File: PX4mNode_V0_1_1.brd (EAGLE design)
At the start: 48.6 x 34.9 mm, 135 parts, among them J201 DF13C-6P-1.25V, J202 DF13C-6P-1.25V, J203 DF13C-6P-1.25V, J301 DF13C-4P-1.25V, J401 DF13C-7P-1.25V, J402 DF13-4P-1.25V, J403 DF13C-4P-1.25V, J404 DF13C-4P-1.25V, J405 DF13C-4P-1.25V, J801 DF13C-3P-1.25V, M3_MOUNT1101 MOUNT-HOLE3.1MM, M3_MOUNT1102 MOUNT-HOLE3.1MM, M3_MOUNT1103 MOUNT-HOLE3.1MM, M3_MOUNT1104 MOUNT-HOLE3.1MM, U101 STM32F4X7VX, U401 MAX3051, U402 MAX3051, X101 3.2x2.5 mm / 24 MHz / 15 ppm

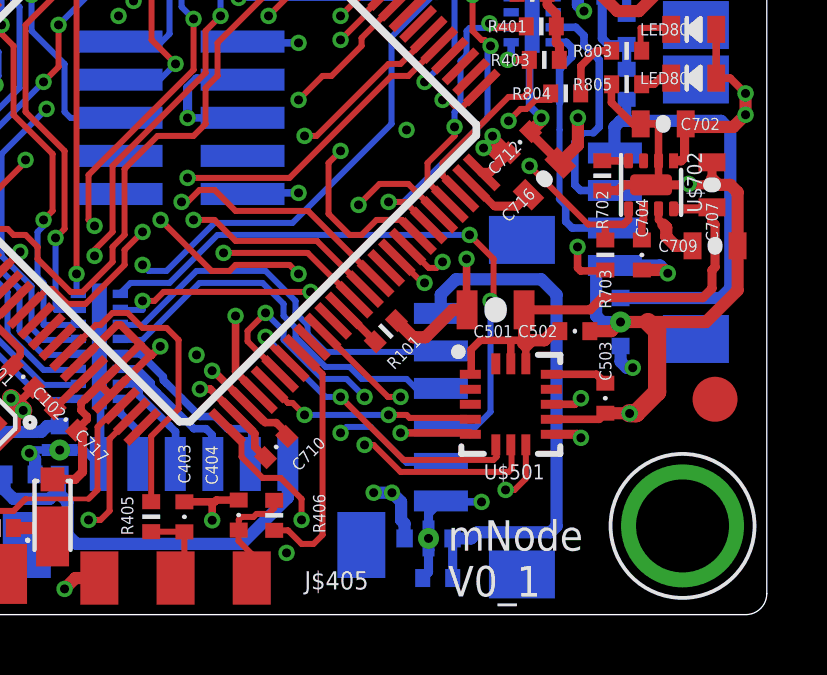
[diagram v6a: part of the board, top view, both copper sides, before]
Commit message: Part renumbering again
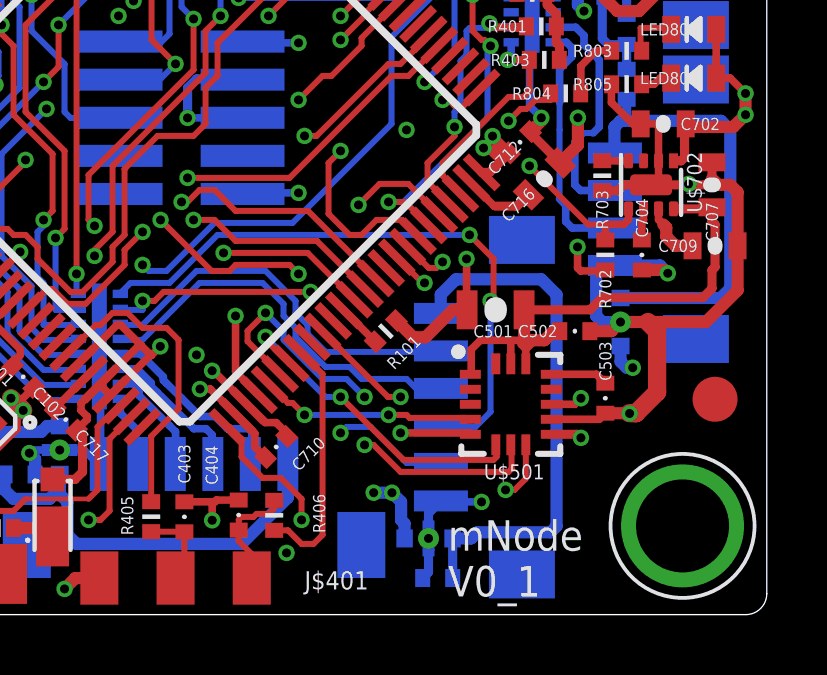
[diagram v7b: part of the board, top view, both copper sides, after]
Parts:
- removed JP2, JP3: FIDUCIAL1.5X3, pixhawk2:FIDUCIAL-1.5X3
- removed U$1: 74LVC2GU04, pixhawk2:SOT363_PHILIPS
- added JP1103, JP1104: FIDUCIAL1.5X3, pixhawk2:FIDUCIAL-1.5X3
- added U$205: PESD0402-140, pixhawk2:0402-TVS
- U$202: value PESD0402-140 -> 74LVC2GU04; device pixhawk2:0402-TVS -> pixhawk2:SOT363_PHILIPS
- moved JP1101 33.0 mm to (51.2, 30.9), flipped to the bottom
- moved U$202 26.1 mm to (22.0, 12.1), turned to 270 degrees
- moved JP1102 25.2 mm to (30.9, 10.2), flipped to the bottom
- moved U$203 14.3 mm to (46.8, 3.96), turned to 0 degrees
- moved U$204 13.0 mm to (32.9, 7.42), turned to 180 degrees
- moved L201 9.08 mm to (35.6, 11.7), turned to 90 degrees
- moved L202 9.08 mm to (26.5, 10.9), turned to 180 degrees
- moved R702 2.64 mm to (52.4, 14.7)
- moved R703 2.64 mm to (52.3, 17.4)
- renumbered C1 to C201, D1 to D701, J$405 to J$401, JP1 to JP201, JP4 to JP202, U$602 to U$601
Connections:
- net 5V_S1_FILTERED: now also U$203.C; no longer U$202.C
- net 5V_S2_FILTERED: now also U$204.C; no longer U$203.C
- net 5V_S3_FILTERED: now also U$205.C; no longer U$204.C
- net FMU-UART7_RX: now also L202.P$5; no longer L201.P$5
- net FMU-UART7_TX: now also L202.P$7; no longer L201.P$7
- net FMU-UART8_RX: now also U$202.6; no longer U$1.6
- net FMU-UART8_TX: now also U$202.3; no longer U$1.3
- net FMU-USART2_CTS: now also L201.P$8; no longer L202.P$8
- net FMU-USART2_RTS: now also L201.P$7; no longer L202.P$7
- net FMU-USART2_RX: now also L201.P$5; no longer L202.P$5
- net FMU-USART2_TX: now also L201.P$6; no longer L202.P$6
- net FMU-USART3_CTS: now also L201.P$2; no longer L202.P$2
- net FMU-USART3_RTS: now also L201.P$1; no longer L202.P$1
- net FMU-USART3_RX: now also L201.P$3; no longer L202.P$3
- net FMU-USART3_TX: now also L201.P$4; no longer L202.P$4
- net FMU-VDD_3V3: now also R702.P$1, U$202.5; no longer R703.P$1, U$1.5
- net GND: now also L202.P$1, L202.P$15, L202.P$16, L202.P$2, R703.P$1, U$202.2, U$205.A; no longer L201.P$1, L201.P$15, L201.P$16, L201.P$2, R702.P$1, U$1.2, U$202.A
- net N$18: now also L202.P$13, L202.P$14; no longer L201.P$13, L201.P$14
- net N$5: now also U$202.4; no longer U$1.4
- net PPM_INPUT: now also L202.P$3, U$202.1; no longer L201.P$3, U$1.1
- net SERIAL1_CTS: now also L201.P$9; no longer L202.P$9
- net SERIAL1_RTS: now also L201.P$10; no longer L202.P$10
- net SERIAL1_RX: now also L201.P$12; no longer L202.P$12
- net SERIAL1_TX: now also L201.P$11; no longer L202.P$11
- net SERIAL2_CTS: now also L201.P$15; no longer L202.P$15
- net SERIAL2_RTS: now also L201.P$16; no longer L202.P$16
- net SERIAL2_RX: now also L201.P$14; no longer L202.P$14
- net SERIAL2_TX: now also L201.P$13; no longer L202.P$13
- net SERIAL3_RX: now also L202.P$12; no longer L201.P$12
- net SERIAL3_TX: now also L202.P$10; no longer L201.P$10
- net SPEKTRUM_RX: now also L202.P$4; no longer L201.P$4
- net VDD_3V3_PERIPH_EN: now also R703.P$2; no longer R702.P$2
- net VDD_3V3_SENSORS_EN: now also R702.P$2; no longer R703.P$2

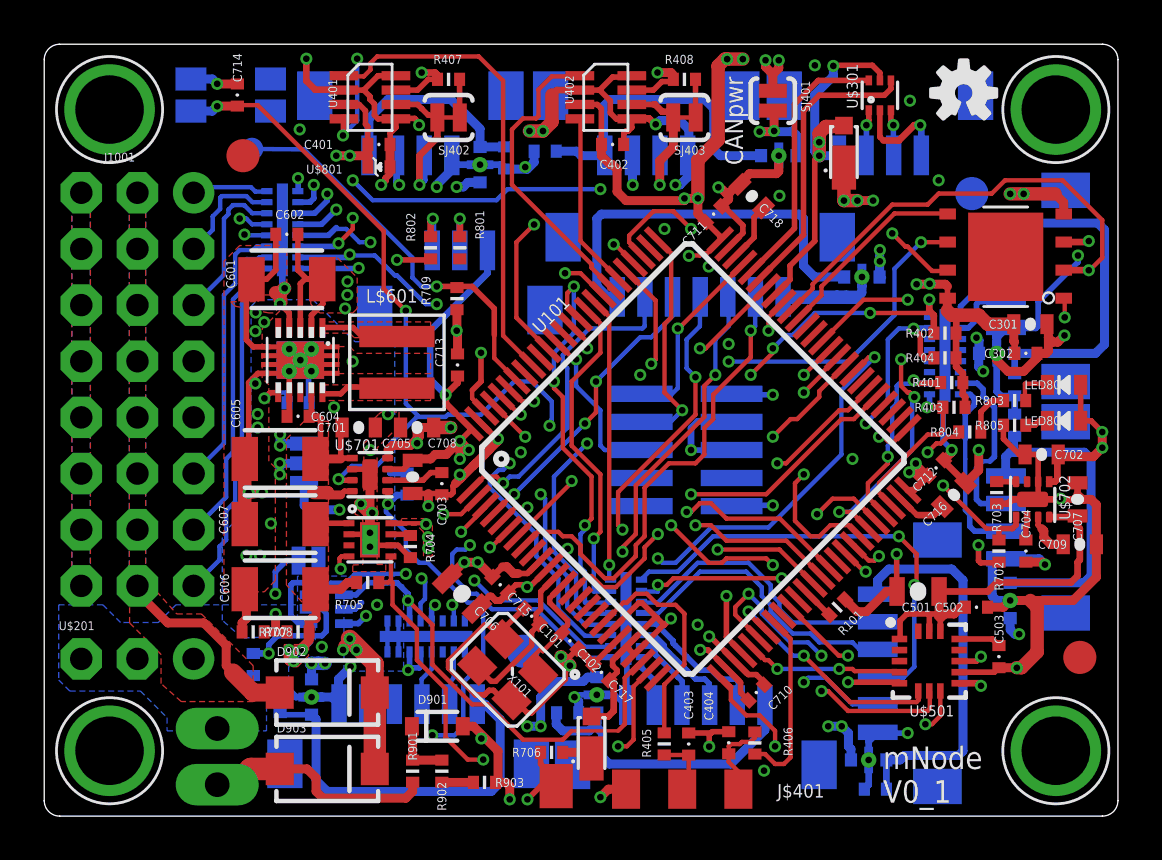
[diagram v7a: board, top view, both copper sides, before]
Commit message: Moved VDD_3V3_SPEKTRUM_EN to a spare ADC to make space for FMU_CH10
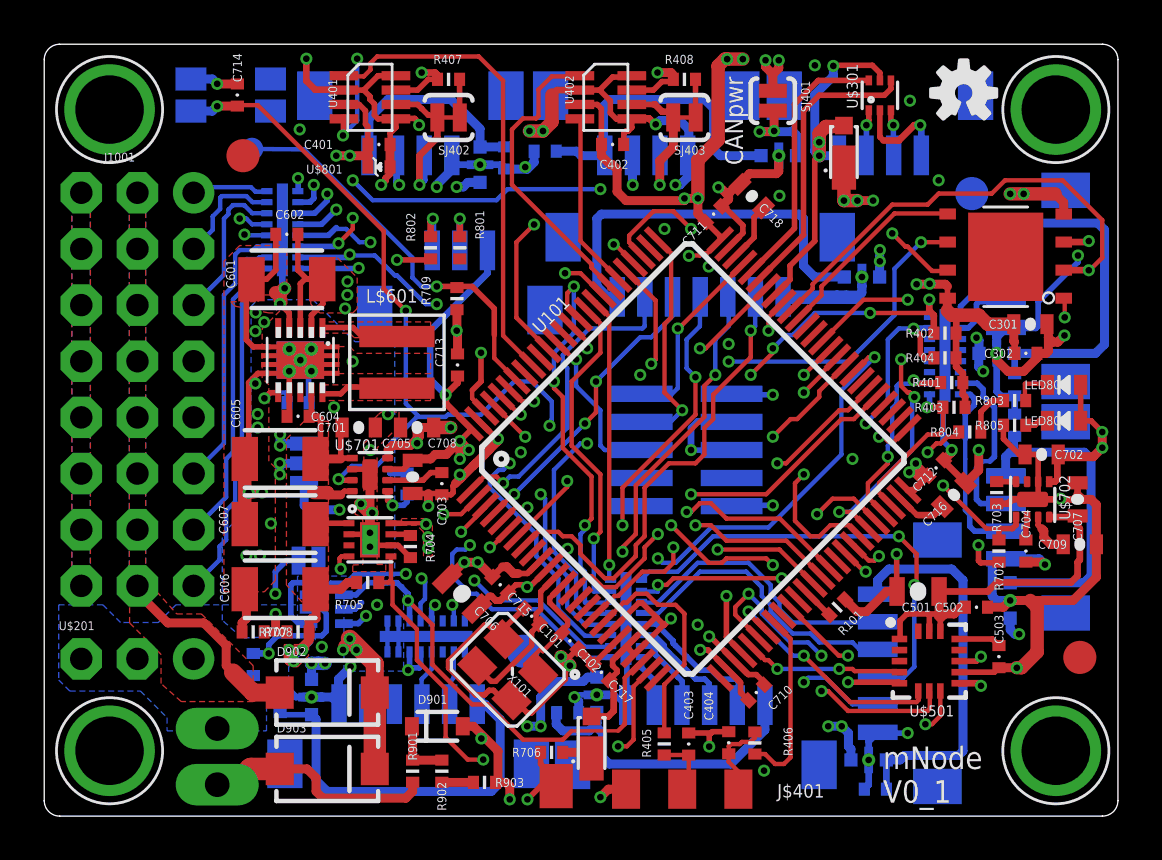
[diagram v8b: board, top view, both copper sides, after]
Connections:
- new net FMU-CH10: U101.26
- net VDD_3V3_SPEKTRUM_EN: now also U101.17; no longer U101.26
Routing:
- net VDD_3V3_SPEKTRUM_EN: track 37.3 -> 21.4 mm, vias 3 -> 2
